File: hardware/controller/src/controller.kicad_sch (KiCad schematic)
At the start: 42 parts, among them J1 Column Connector, J2 Row Connector, J3 12V DC Barrel Jack, J4 USB C, J5 Conn_01x02, SW1 RESET, SW2 BOOT, U1 ESP32-S3-WROOM-1, U2 XL1509-5.0, U3 XC6206P332MR, U4 MT9700

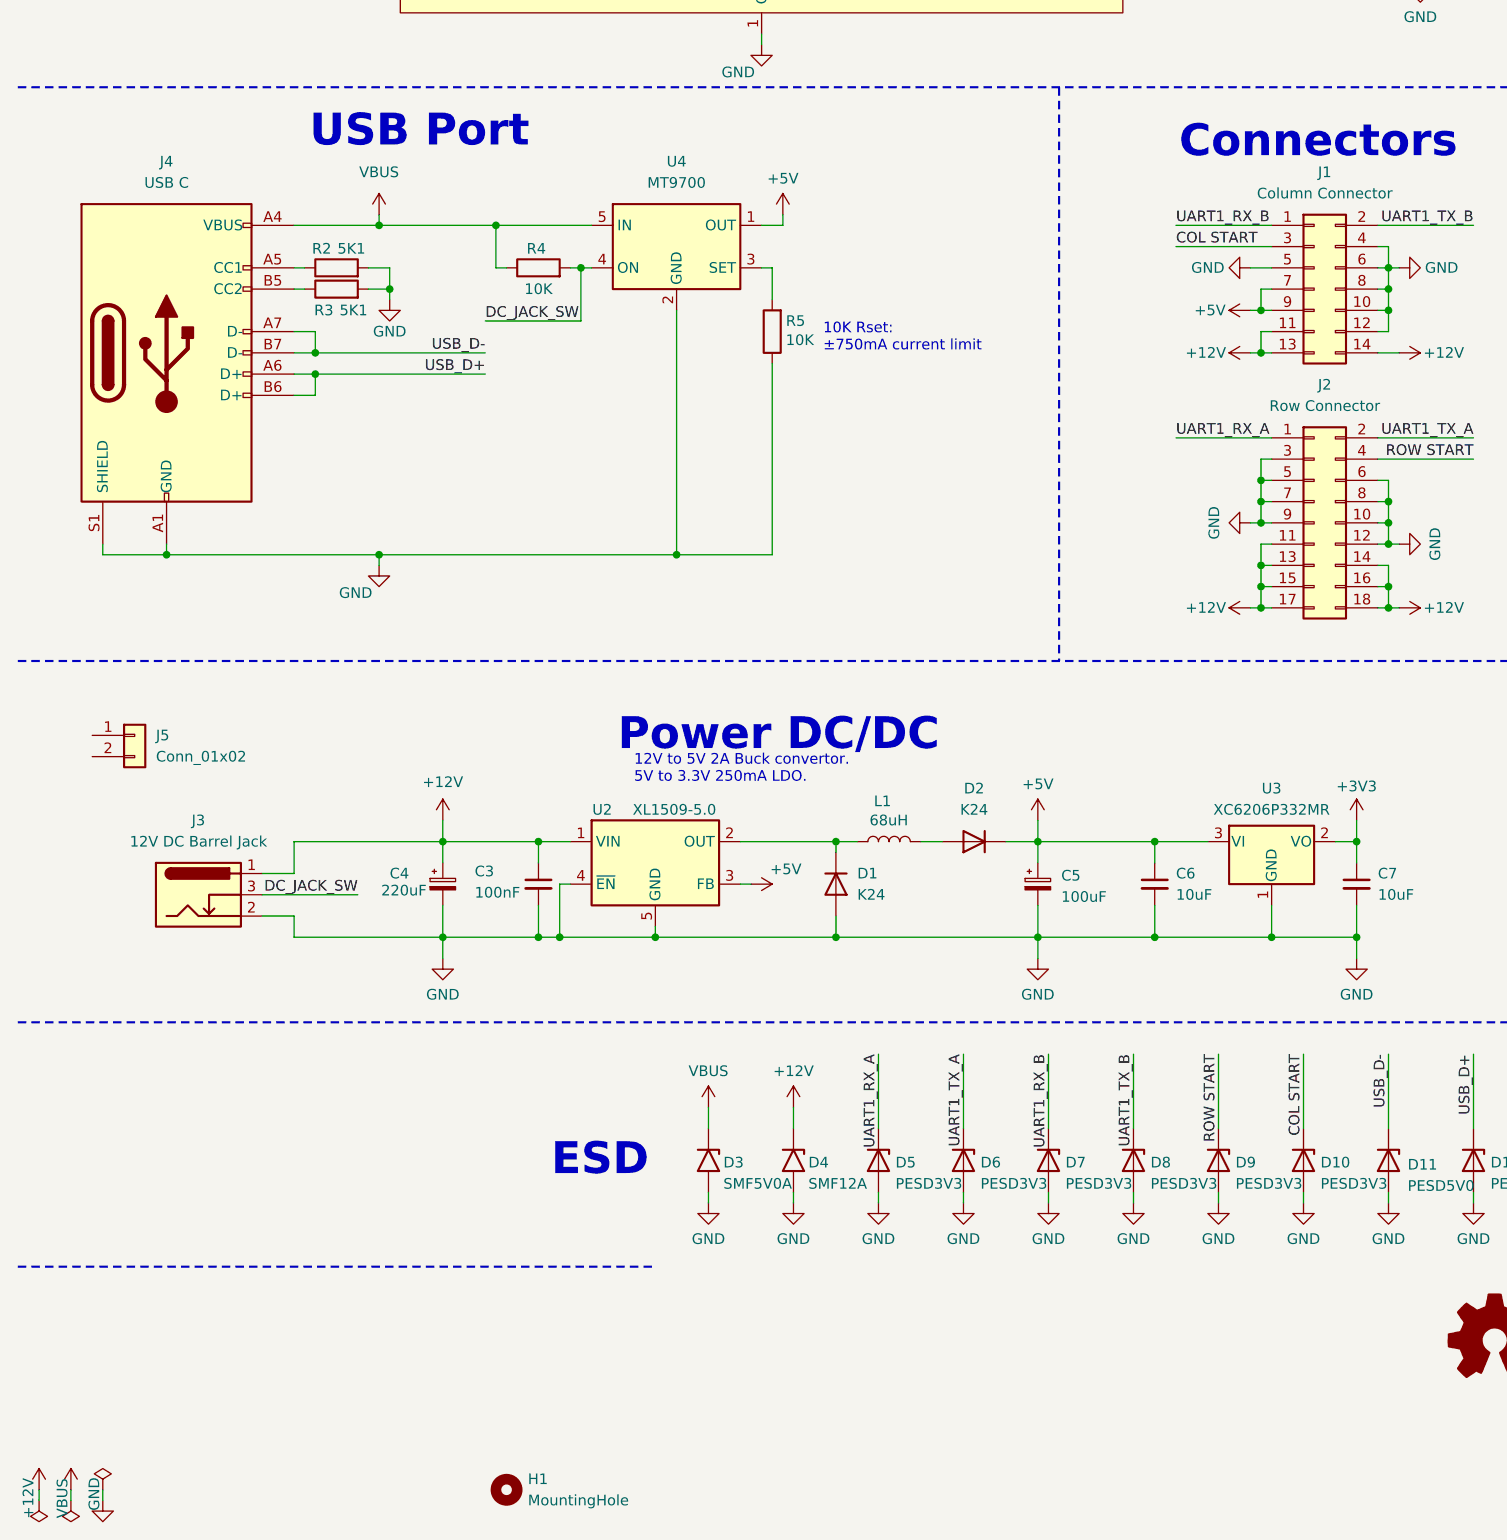
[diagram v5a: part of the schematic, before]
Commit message: Change barel jack for XT30 connector and bump LDO to 600mA, remove usb power switch  in favor of diode.
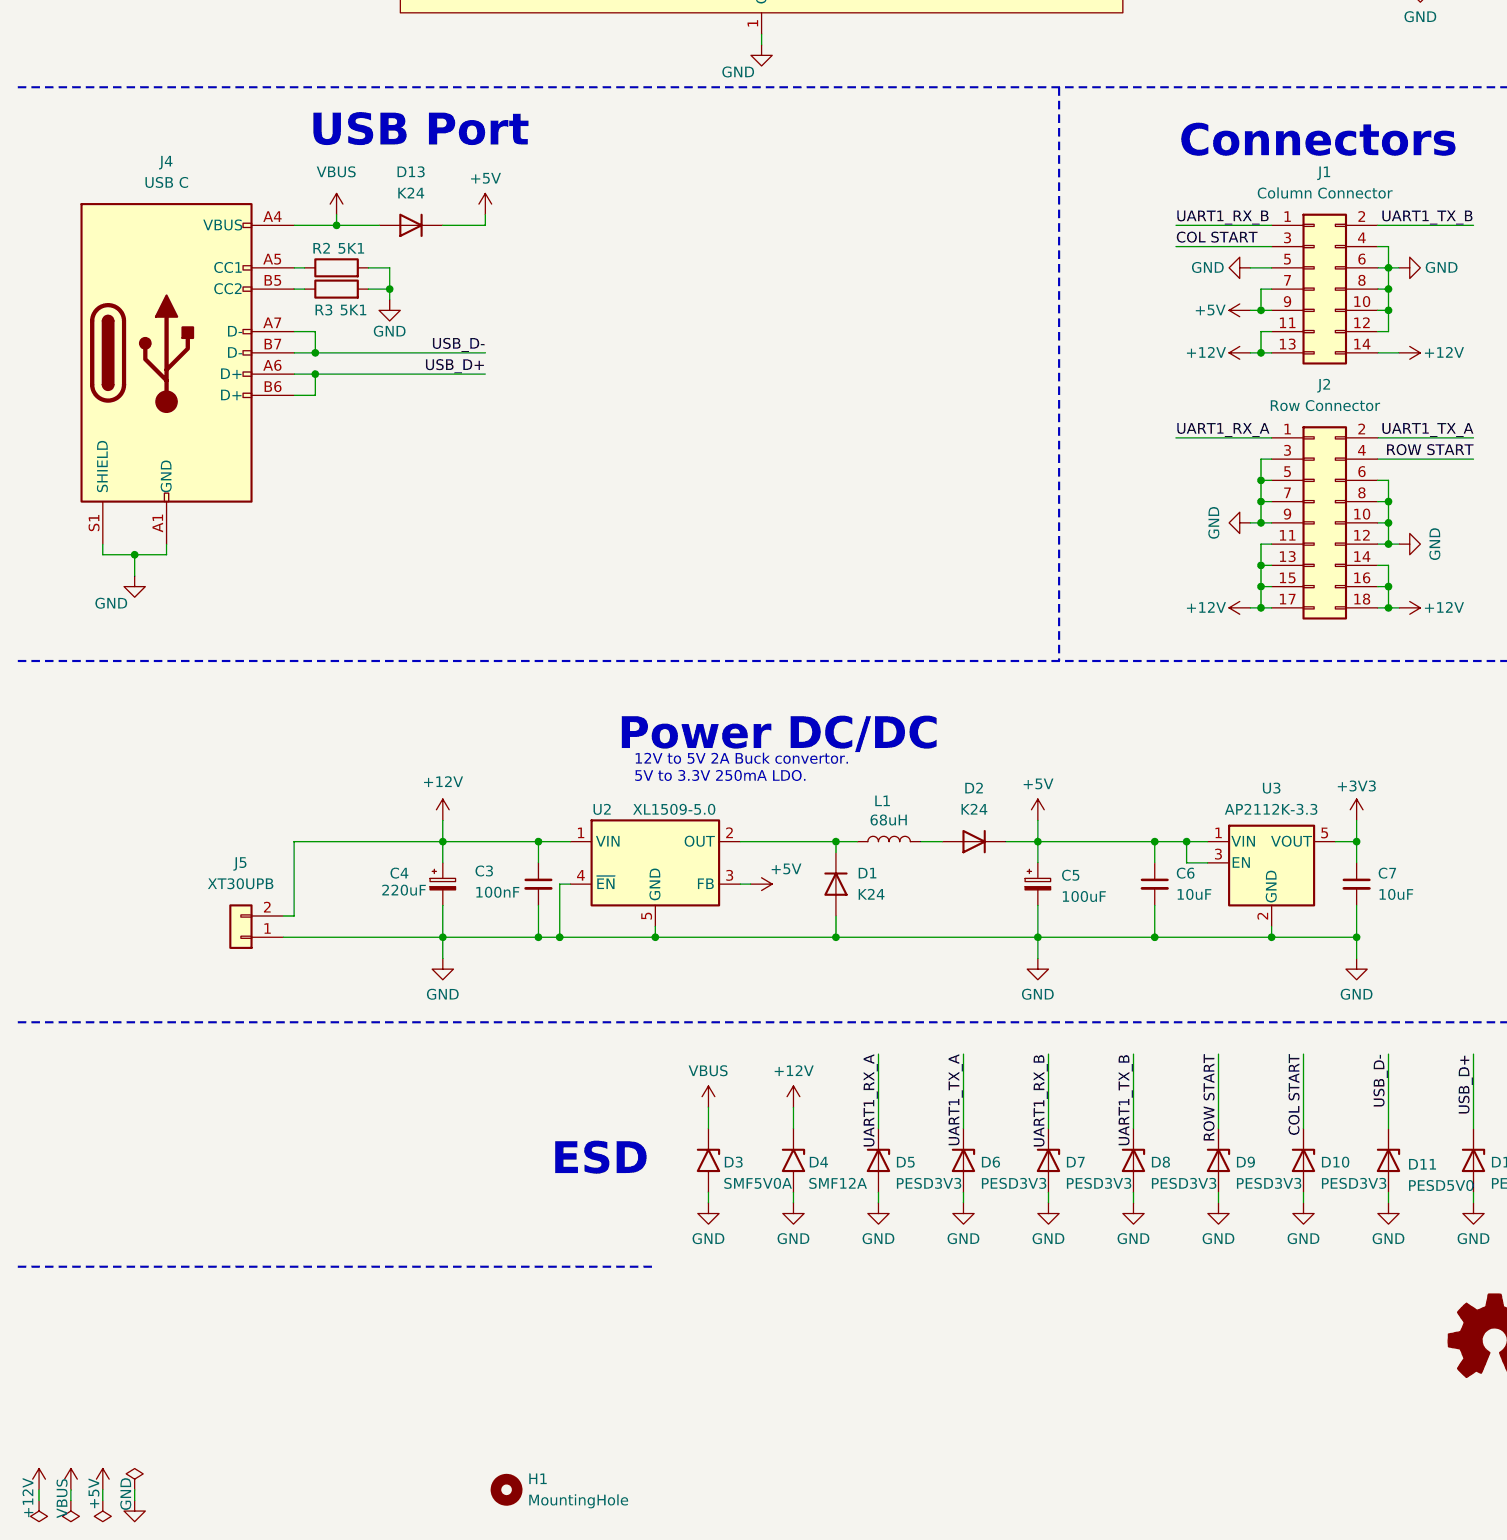
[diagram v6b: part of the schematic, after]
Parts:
- removed J3: 12V DC Barrel Jack, DC-jack-connector:DC-012A-25A, symbol Connector:Barrel_Jack_Switch
- removed R4, R5: 10K, Resistor_SMD:R_0603_1608Metric, symbol Device:R
- removed U3: XC6206P332MR, Package_TO_SOT_SMD:SOT-23-3, symbol Regulator_Linear:XC6206PxxxMR
- removed U4: MT9700, Package_TO_SOT_SMD:SOT-23-5, symbol Power_Management:AAT4610BIGV-1-T1
- added D13: K24, Diode_SMD:D_SMF, symbol Device:D
- added U3: AP2112K-3.3, Package_TO_SOT_SMD:SOT-23-5, symbol Regulator_Linear:AP2112K-3.3
- J5: value Conn_01x02 -> XT30UPB; footprint Connector_AMASS:AMASS_XT30U-M_1x02_P5.0mm_Vertical -> Connector_AMASS:AMASS_XT30UPB-M_1x02_P5.0mm_Vertical; LCSC (none) -> C428721
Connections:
- net +12V: now also J5.2 (Pin_2)
- net +3V3: now also U3.5 (VOUT)
- net +5V: now also D13.1 (K), U3.1 (VIN), U3.3 (EN)
- net GND: now also J5.1 (Pin_1), U3.2 (GND)
- net VBUS: now also D13.2 (A)
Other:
- note removed: "10K Rset: ±750mA current limit"
- moved on the sheet: J5

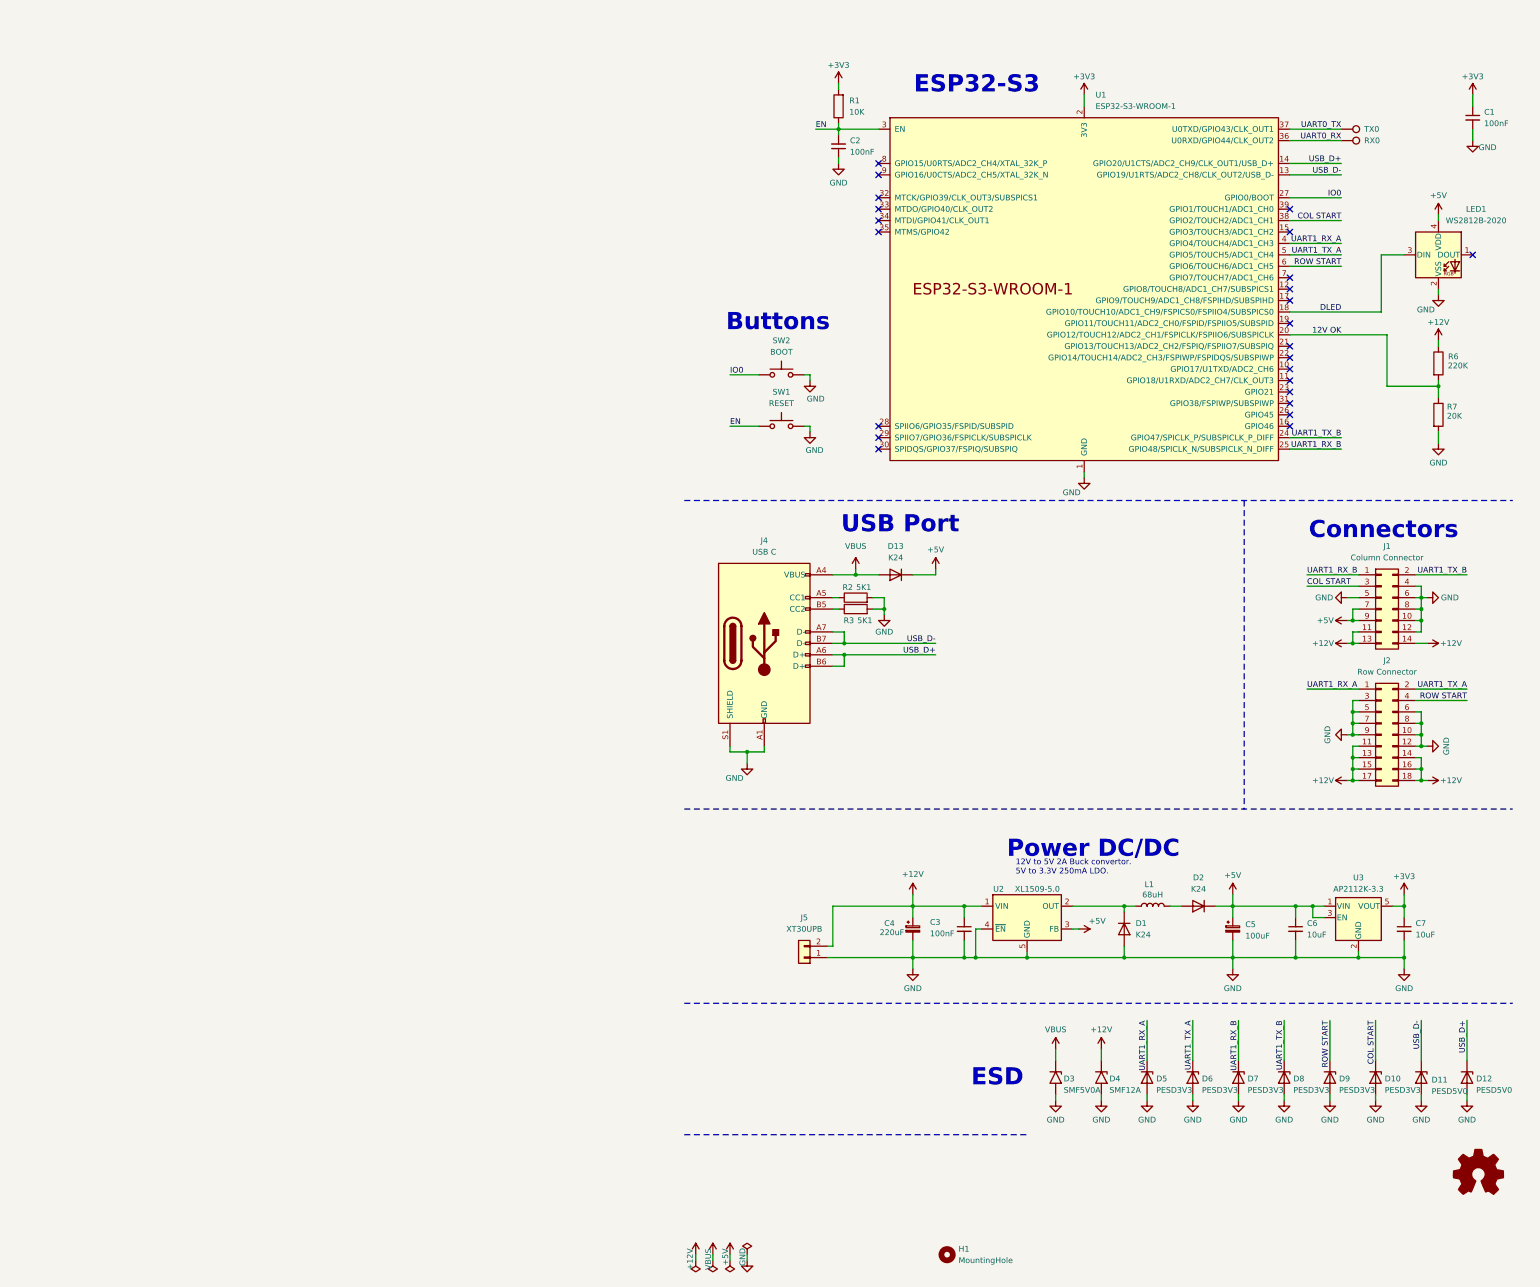
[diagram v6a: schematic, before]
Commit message: Add test points to pcb's
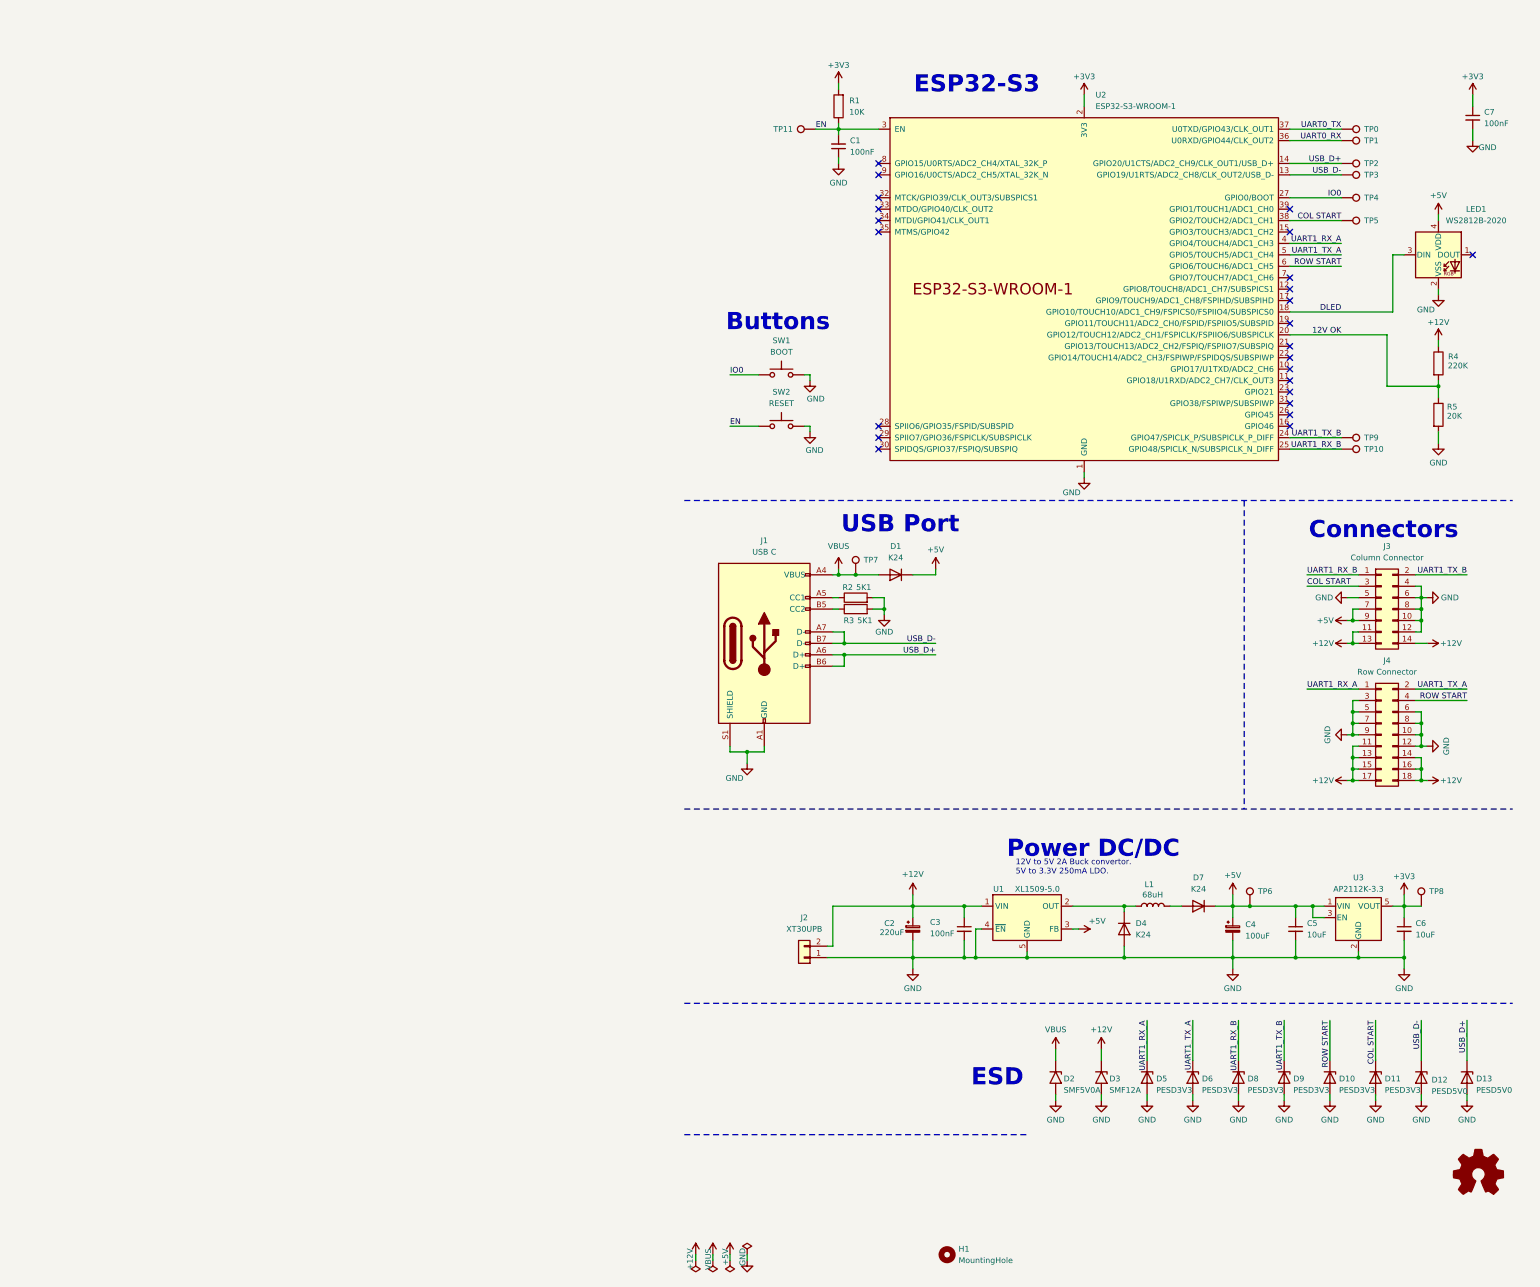
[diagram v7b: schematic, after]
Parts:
- removed RX0: TestPoint, TestPoint:TestPoint_Pad_D1.5mm, symbol Connector:TestPoint
- added TP1, TP10, TP11, TP2, TP3, TP4, TP5, TP6, TP7, TP8, TP9: TestPoint, TestPoint:TestPoint_Pad_D1.5mm, symbol Connector:TestPoint
- renumbered C2 to C1, C4 to C2, C5 to C4, C6 to C5, C7 to C6, C1 to C7, D13 to D1, D9 to D10, D10 to D11, D11 to D12, D12 to D13, D3 to D2, D4 to D3, D1 to D4, D2 to D7, D7 to D8, D8 to D9, J4 to J1, J5 to J2, J1 to J3, J2 to J4, R6 to R4, R7 to R5, SW2 to SW1, SW1 to SW2, TX0 to TP0, U2 to U1, U1 to U2
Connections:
- net +3V3: now also TP8.1
- net +5V: now also TP6.1
- net COL START: now also TP5.1
- net EN: now also TP11.1
- net IO0: now also TP4.1
- net UART0_RX: now also TP1.1
- net UART1_RX_B: now also TP10.1
- net UART1_TX_B: now also TP9.1
- net USB_D+: now also TP2.1
- net USB_D-: now also TP3.1
- net VBUS: now also TP7.1

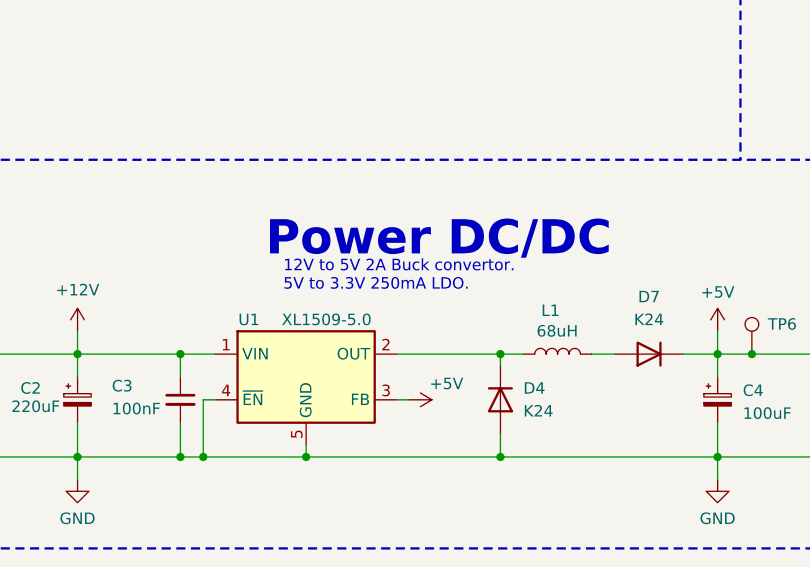
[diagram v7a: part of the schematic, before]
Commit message: Update note in schematic
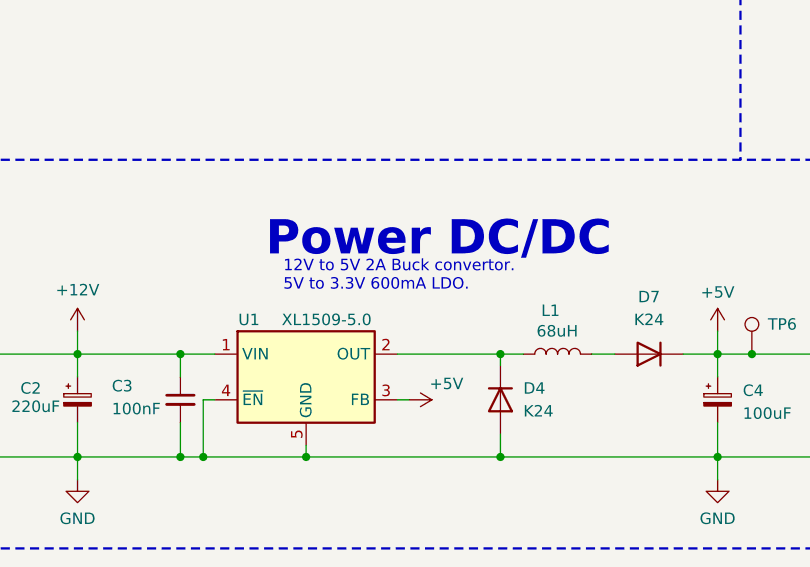
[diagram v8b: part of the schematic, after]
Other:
- note added: "12V to 5V 2A Buck convertor. 5V to 3.3V 600mA LDO."
- note removed: "12V to 5V 2A Buck convertor. 5V to 3.3V 250mA LDO."
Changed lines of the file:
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@@
 		)
 	)
-	(text "12V to 5V 2A Buck convertor.\n5V to 3.3V 250mA LDO."
+	(text "12V to 5V 2A Buck convertor.\n5V to 3.3V 600mA LDO."
 		(exclude_from_sim no)
 		(at 86.36 193.294 0)
